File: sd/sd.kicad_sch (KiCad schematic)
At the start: 18 parts, among them J1 Micro_SD_Card_Det2, J3 STM32WORLD_BOARD, J4 STM32WORLD_CONNECTOR_1, J5 STM32WORLD_CONNECTOR_2

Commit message: Working on sd
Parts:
- added JP10, JP11, JP12, JP13, JP14, JP15, JP16, JP17, JP18, JP19, JP20, JP21, JP22, JP7, JP8, JP9: SolderJumper_2_Open, Jumper:SolderJumper-2_P1.3mm_Open_TrianglePad1.0x1.5mm, symbol Jumper:SolderJumper_2_Open
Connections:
- net CMD is gone; now on net SD_DAT3: R3.2
- net D0 is gone; now on net SD_CMD: R4.2
- net D1 is gone; now on net SD_DAT0: R5.2
- net D2 is gone; now on net SDIO_DAT2: R1.2
- net D3 is gone; now on net SDIO_DAT1: R2.2
- net DET: now also J5.35 (PC15)
- net SDIO_CLK: now also J5.22 (PC12), JP18.2 (B)
- net SDIO_CMD: now also J5.24 (PD2)
- net SDIO_DAT0: now also J4.32 (PC8)
- net SDIO_DAT1: now also J4.31 (PC9)
- net SDIO_DAT2: now also J5.20 (PC10), JP14.2 (B)
- net SDIO_DAT3: now also J5.19 (PC11), JP22.2 (B)
- net SPI_CLK: now also JP11.1 (A), JP12.1 (A), JP13.1 (A), JP14.1 (A)
- net SPI_CS: now also JP10.1 (A), JP7.1 (A), JP8.1 (A), JP9.1 (A)
- net SPI_MISO: now also JP19.1 (A), JP20.1 (A), JP21.1 (A), JP22.1 (A)
- net SPI_MOSI: now also JP15.1 (A), JP16.1 (A), JP17.1 (A), JP18.1 (A)
- net SPI1A_CS: now reaches J5.15 (PA15)
- net SPI1A_CS: now also JP8.2 (B)
- net SPI1A_CLK: now reaches J5.23 (PB3)
- net SPI1A_CLK: now also JP12.2 (B)
- net SPI1A_MOSI: now reaches J5.25 (PB5)
- net SPI1A_MOSI: now also JP16.2 (B)
- net SPI1A_MISO: now reaches J5.26 (PB4)
- net SPI1A_MISO: now also JP20.2 (B)
- net SPI2_MOSI: now reaches J4.11 (PA3)
- net SPI2_MOSI: now also JP17.2 (B)
- net SPI1_CLK: now reaches J4.13 (PA5)
- net SPI1_CLK: now also JP11.2 (B)
- net SPI1_CS: now reaches J4.14 (PA4)
- net SPI1_CS: now also JP10.2 (B), JP7.2 (B)
- net SPI1_MOSI: now reaches J4.15 (PA7)
- net SPI1_MOSI: now also JP15.2 (B)
- net SPI1_MISO: now reaches J4.16 (PA6)
- net SPI1_MISO: now also JP19.2 (B)
- net SPI2_CLK: now reaches J4.24 (PB10)
- net SPI2_CLK: now also JP13.2 (B)
- net SPI2_CS: now reaches J4.26 (PB12)
- net SPI2_CS: now also JP9.2 (B)
- net SPI2_MISO: now reaches J4.8 (PC2)
- net SPI2_MISO: now also JP21.2 (B)
- no-connect marks 0 -> 2
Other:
- moved on the sheet: C1, C2, J1, J4, J5, JP1, JP2, JP3, JP4, JP5, JP6, R1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

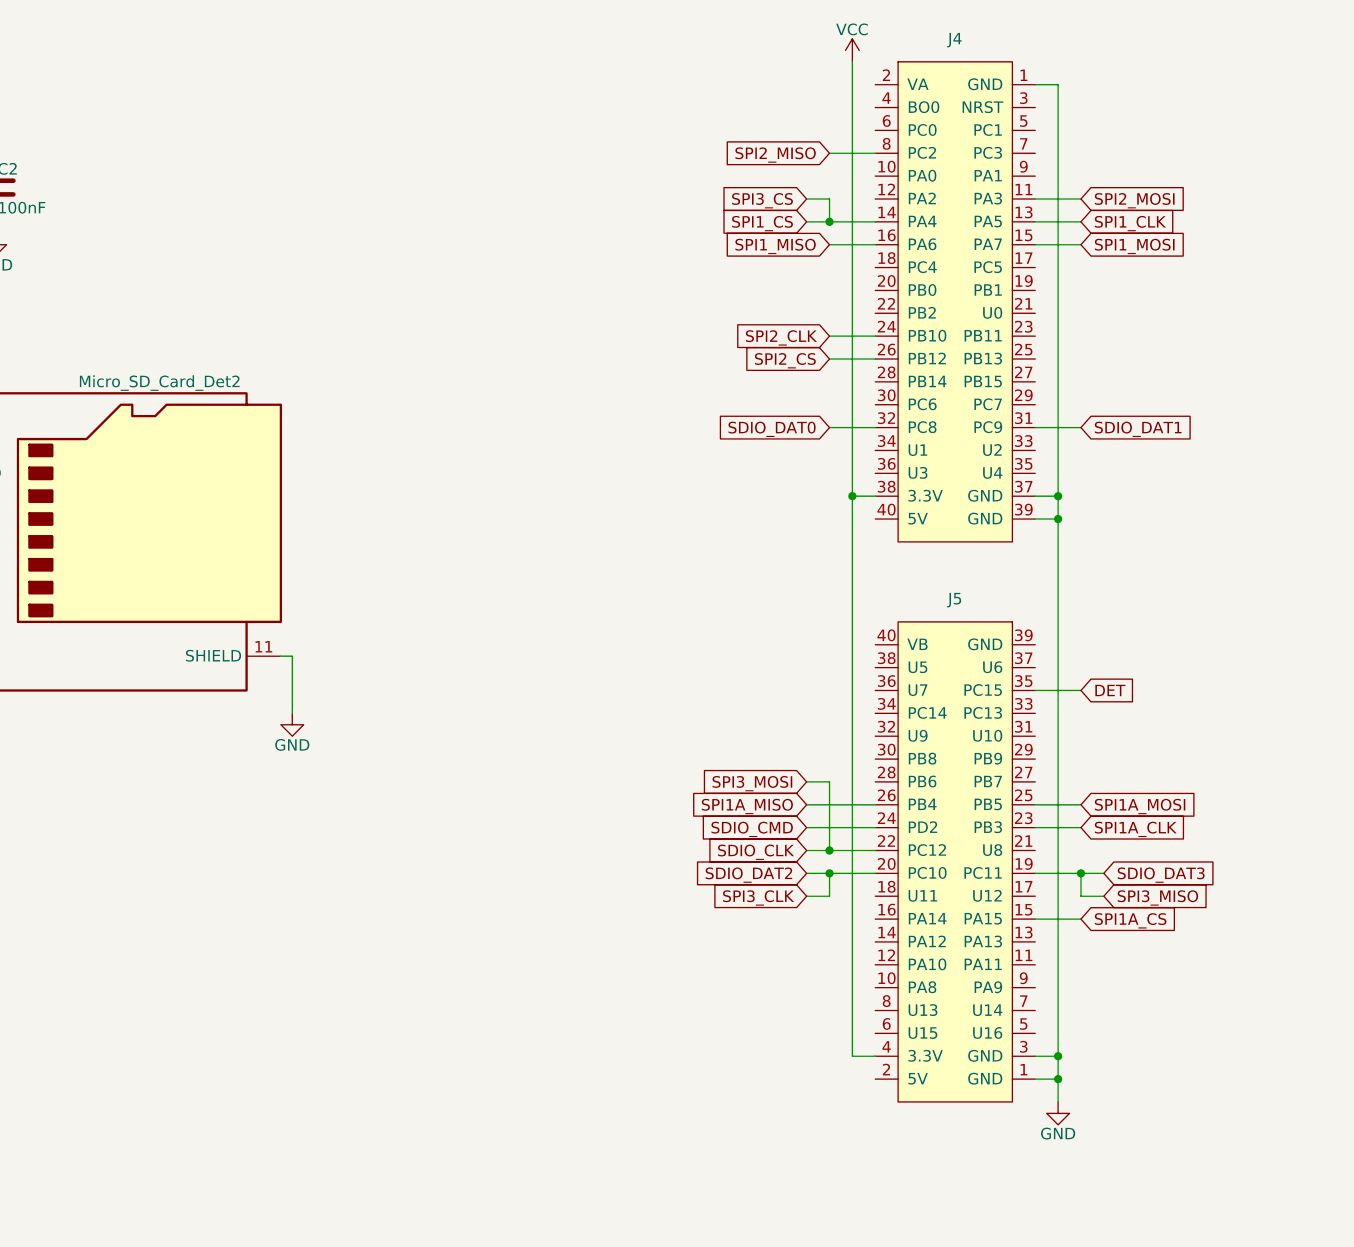
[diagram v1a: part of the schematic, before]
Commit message: Schematics verified- tweaking pcb
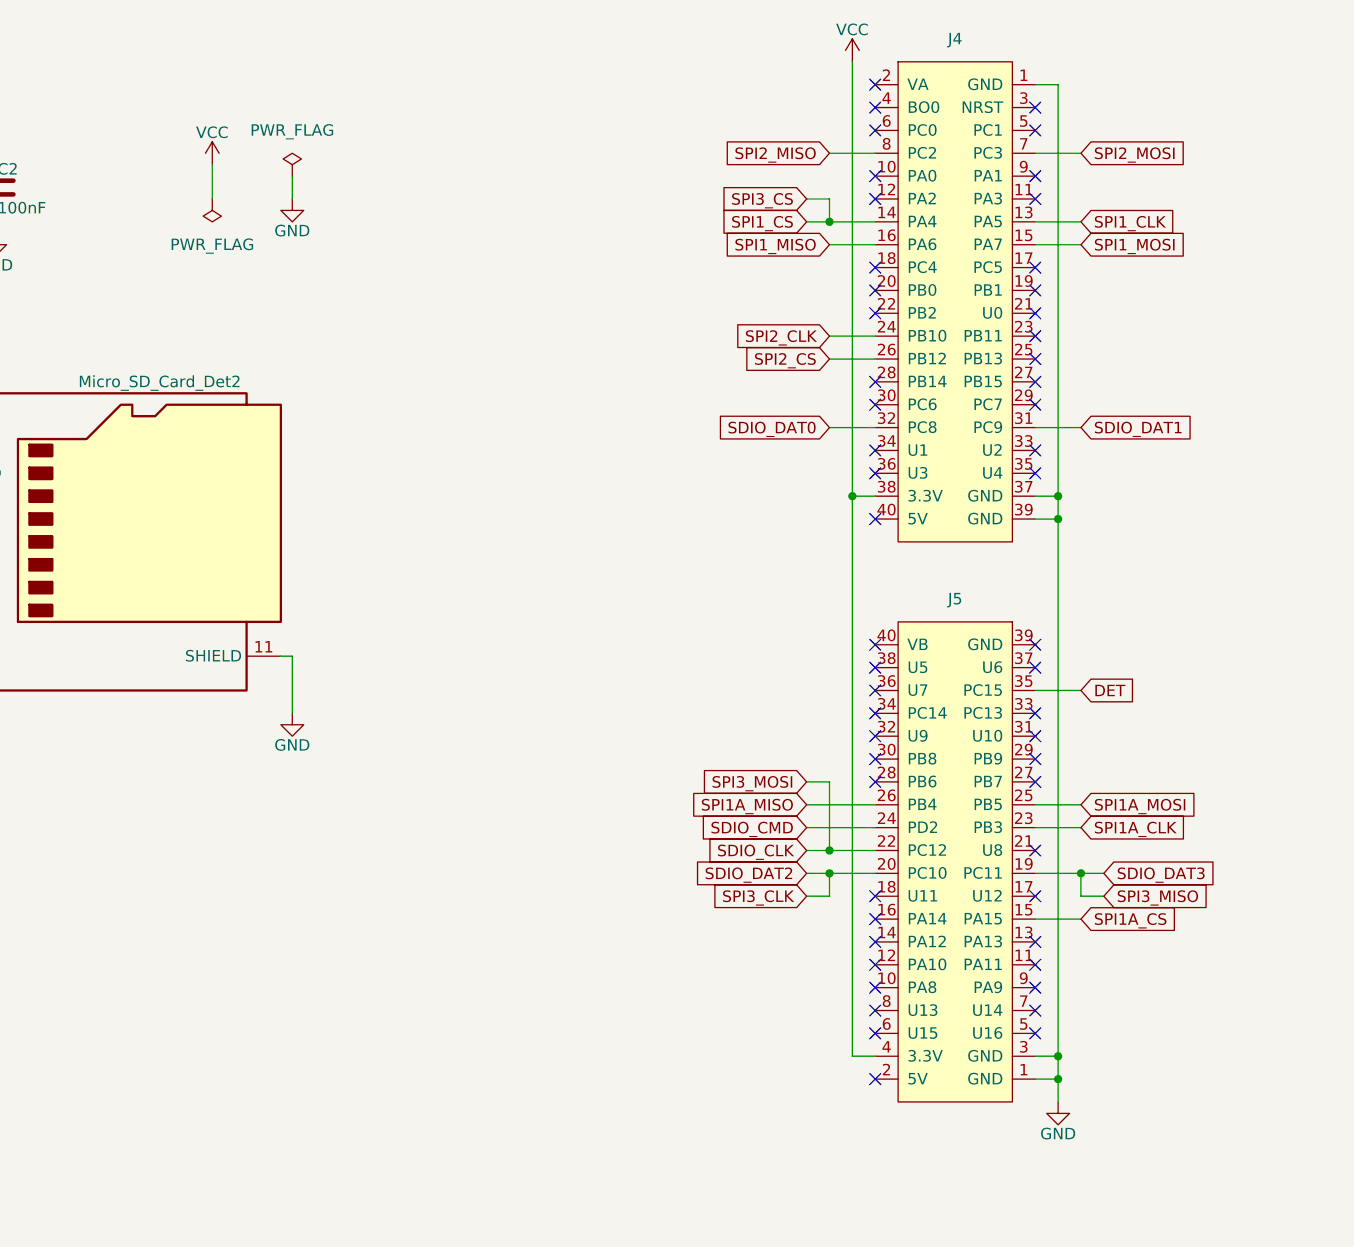
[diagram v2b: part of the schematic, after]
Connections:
- net SPI2_MOSI: now also J4.7 (PC3); no longer J4.11 (PA3)
- no-connect marks 2 -> 56

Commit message: Ordered sd rev a
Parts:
- C1: LCSC C719027 -> C1588
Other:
- moved on the sheet: C1, C2, J1, JP1, JP2, JP3, JP4, JP5, JP6, R1, R2, R3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
